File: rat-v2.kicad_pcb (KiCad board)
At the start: 2 copper layers, 56 x 60 mm, 57 parts, among them P1 9V, P2 LED-, P3 GND, P4 IN, P5 GND, P6 OUT, P7 GND, P8 GND, Q1 2N5458, SW1 SW_DPDT_x2, SW2 SW_DPDT_x2, U2 LM301

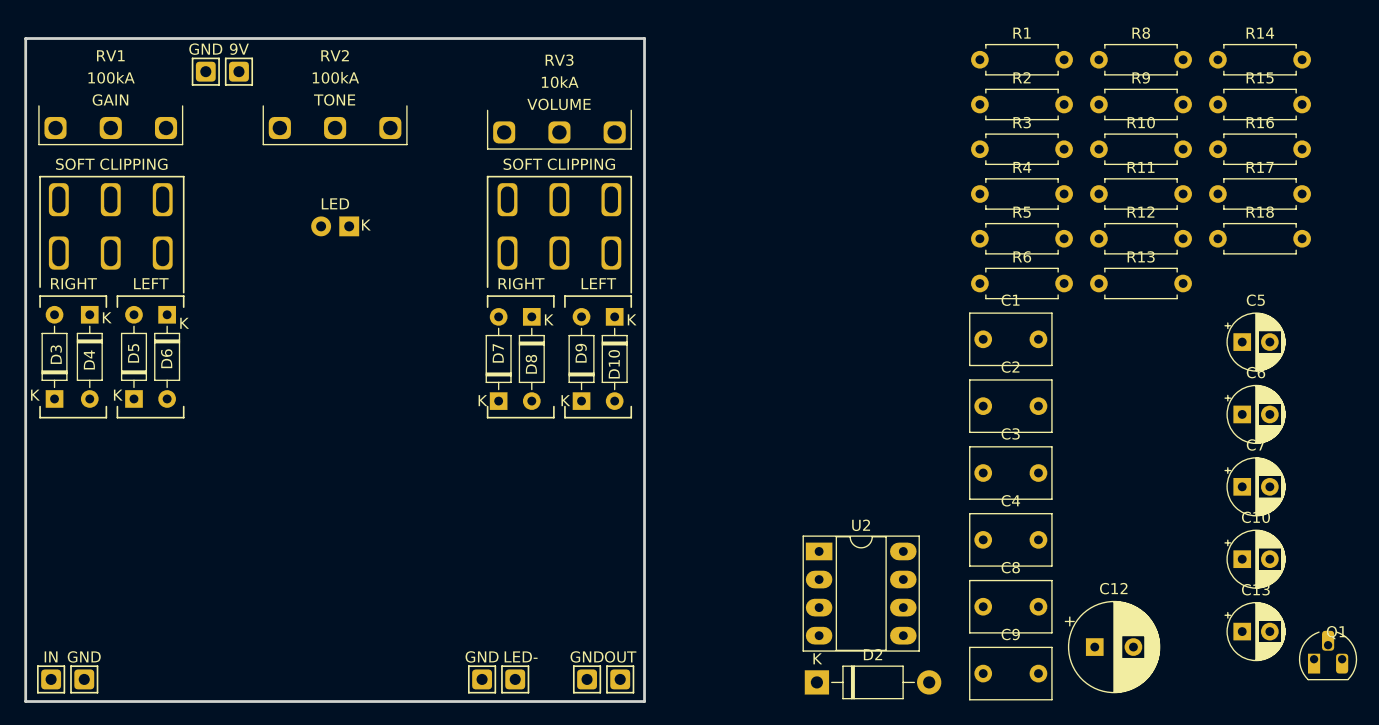
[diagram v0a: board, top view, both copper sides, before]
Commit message: Placement just about done
might need some minor tweaking
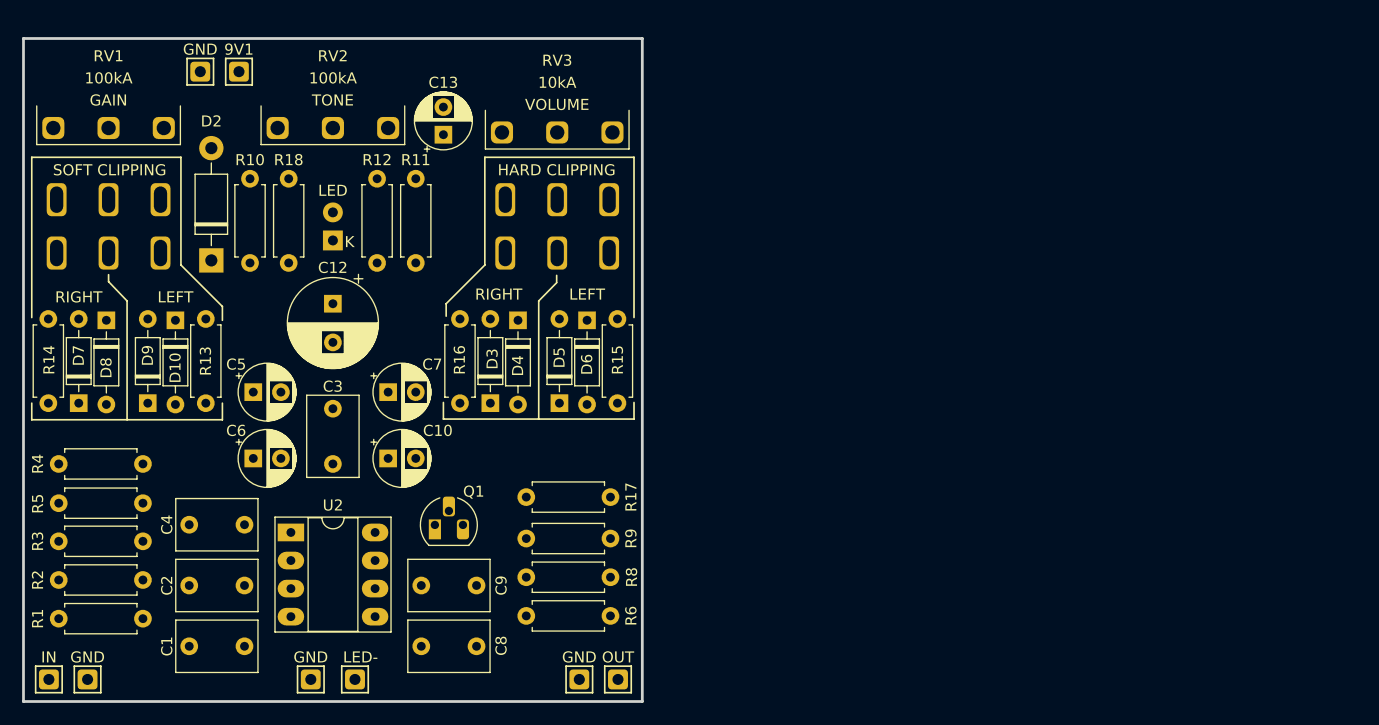
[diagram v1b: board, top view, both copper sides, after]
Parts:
- P1: value 9V -> 9V1
- moved R14 110.3 mm to (57.2, 114.0), turned to 90 degrees
- moved R1 97.5 mm to (58.2, 133.5)
- moved R3 90.6 mm to (58.2, 126.5)
- moved C5 89.6 mm to (75.8, 113.0)
- moved C6 89.6 mm to (75.8, 119.0)
- moved R2 87.1 mm to (65.8, 130.0), turned to 180 degrees
- moved C13 85.1 mm to (93.0, 89.7), turned to 90 degrees
- moved R18 84.3 mm to (79.0, 93.7), turned to -90 degrees
- moved R13 81.5 mm to (71.5, 114.0), turned to 90 degrees
- moved Q1 80.5 mm to (92.2, 125.0)
- moved R4 79.6 mm to (65.8, 119.5), turned to 180 degrees
- moved R5 79.4 mm to (65.8, 123.0), turned to 180 degrees
- moved C10 77.8 mm to (88.0, 119.0)
- moved C7 77.8 mm to (88.0, 113.0)
- moved R10 76.9 mm to (75.5, 93.7), turned to -90 degrees
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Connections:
- net Net-(C1-Pad1) renamed /IN
- net Net-(C1-Pad2) renamed /IN_AC
- net Net-(C10-Pad2) renamed /SRC_AC
- net Net-(C8-Pad2) renamed /TONE_F
- net Net-(D10-A) renamed /OP_OUT
- net Net-(P1-Pad1) renamed +9VIN
- net Net-(P6-Pad1) renamed /OUT
- net Net-(Q1-G) renamed /GATE
- net Net-(Q1-S) renamed /SRC
- net Net-(R6-Pad2) renamed /TONE
- net Net-(SW1A-B) renamed /HRD_CLP
- net Net-(SW2A-B) renamed /FB
- net Net-(U2-+) renamed /IN_F
- net Net-(U2-BAL) renamed /COMP-
- net Net-(U2-C/B) renamed /COMP+
- P8 pad 1: (no net) -> GND
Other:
- board text added: "HARD CLIPPING"

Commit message: Ship It?
I think it is finished. Error free. Haven't generated BOM or files
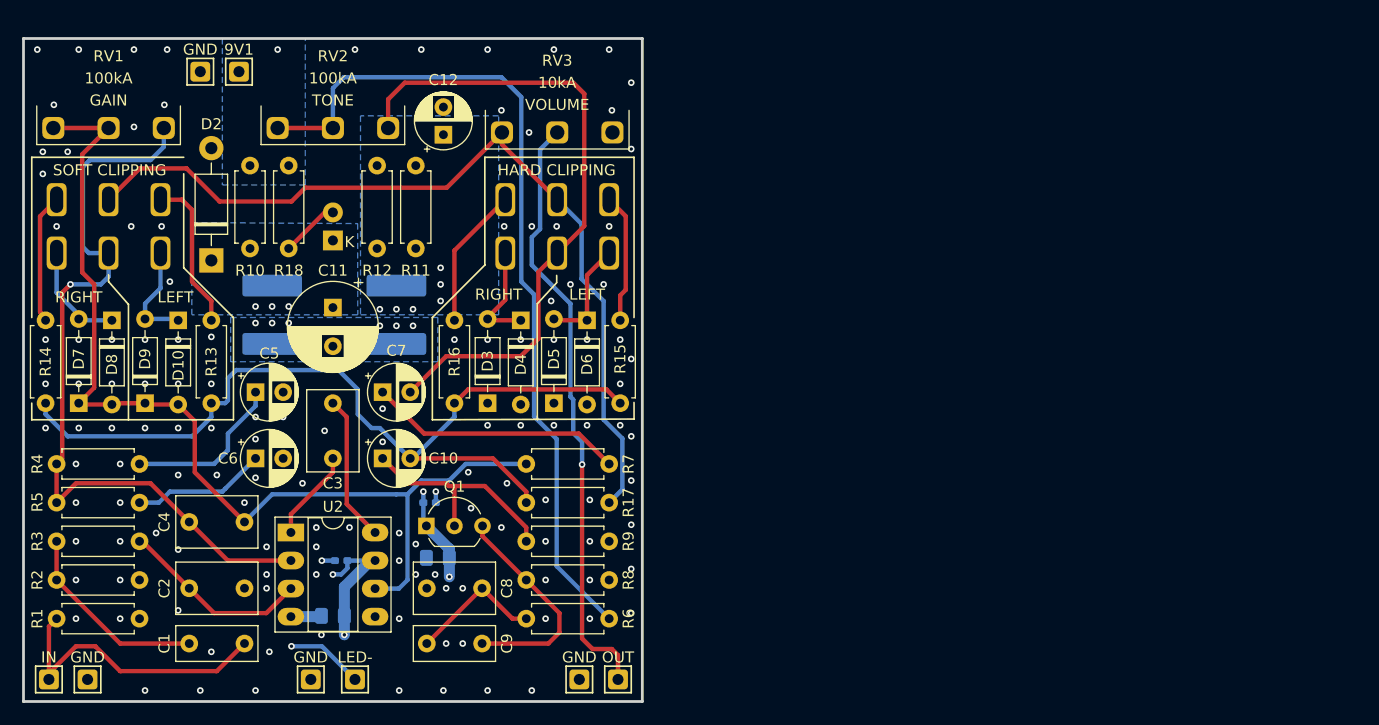
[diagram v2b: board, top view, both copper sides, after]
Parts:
- removed the REF** at (67.8, 52.0)
- removed the REF** at (98.2, 52.0)
- added C13: 1u, Capacitor_SMD:C_0805_2012Metric_Pad1.18x1.45mm_HandSolder, B.Cu at (83.0, 133.2)
- added C14: 1u, Capacitor_SMD:C_0805_2012Metric_Pad1.18x1.45mm_HandSolder, B.Cu at (92.5, 128.0)
- added C15: 100n, Capacitor_SMD:C_0402_1005Metric_Pad0.74x0.62mm_HandSolder, B.Cu at (83.8, 128.2)
- added C16: 100n, Capacitor_SMD:C_0402_1005Metric_Pad0.74x0.62mm_HandSolder, B.Cu at (91.8, 123.0)
- added C17: 10u, Capacitor_SMD:C_2220_5750Metric_Pad1.97x5.40mm_HandSolder, B.Cu at (77.5, 106.0)
- added C18: 10u, Capacitor_SMD:C_2220_5750Metric_Pad1.97x5.40mm_HandSolder, B.Cu at (88.8, 106.0)
- added R7: 1.5k, BB_Resistors:R_Axial_DIN0207_L6.3mm_D2.5mm_P7.5mm_Horizontal, F.Cu at (108.0, 119.5)
- added REF**: Jack_0.25in_Solder_MechOnly, BB_Jacks:Jack_0.25in_Solder_MechOnly, F.Cu at (98.4, 52.8)
- added REF**: Jack_0.25in_Solder_MechOnly, BB_Jacks:Jack_0.25in_Solder_MechOnly, F.Cu at (68.0, 52.8)
- C1, C9: footprint Capacitor_THT:C_Rect_L7.2mm_W4.5mm_P5.00mm_FKS2_FKP2_MKS2_MKP2 -> Capacitor_THT:C_Rect_L7.2mm_W3.0mm_P5.00mm_FKS2_FKP2_MKS2_MKP2
- C3: value 30p -> 47p
- Q1: footprint Package_TO_SOT_THT:TO-92_HandSolder -> Package_TO_SOT_THT:TO-92_Inline_Wide
- R1, R2: value 1M -> 2.2M; footprint Resistor_THT:R_Axial_DIN0207_L6.3mm_D2.5mm_P7.62mm_Horizontal -> BB_Resistors:R_Axial_DIN0207_L6.3mm_D2.5mm_P7.5mm_Horizontal
- R10, R11, R12, R13, R14, R15, R16, R17, R18, R3, R4, R5, R6, R8, R9: footprint Resistor_THT:R_Axial_DIN0207_L6.3mm_D2.5mm_P7.62mm_Horizontal -> BB_Resistors:R_Axial_DIN0207_L6.3mm_D2.5mm_P7.5mm_Horizontal
- moved C8 6.91 mm to (91.5, 130.8), turned to 0 degrees
- moved C9 5.27 mm to (91.5, 135.8)
- moved R12 1.31 mm to (87.0, 100.0)
- moved R10 1.19 mm to (75.5, 92.5)
- moved R11 1.19 mm to (90.5, 92.5)
- moved R18 1.19 mm to (79.0, 92.5)
- moved REF** 1.02 mm to (83.0, 51.0)
- moved Q1 0.78 mm to (91.5, 125.1)
- moved C10 0.50 mm to (87.5, 119.0)
- moved C3 0.50 mm to (83.0, 114.0)
- moved C7 0.50 mm to (87.5, 113.0)
- moved D5 0.50 mm to (103.0, 114.0)
- moved D8 0.50 mm to (63.0, 106.5)
- moved R13 0.50 mm to (72.0, 114.0)
- moved R16 0.50 mm to (94.0, 114.0)
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- renumbered C12 to C11, C13 to C12
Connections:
- C7 pad 1: /OP_OUT -> /OP_OUT_R
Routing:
- net /OP_OUT: track 0.00 -> 92.9 mm
- net /SRC_AC: track 0.00 -> 79.4 mm
- net Net-(SW1B-B): track 0.00 -> 79.1 mm
- net /TONE: track 0.00 -> 77.3 mm
- net Net-(D1-K): track 0.00 -> 72.2 mm, vias 0 -> 1
- net /FB: track 0.00 -> 71.2 mm, vias 0 -> 1
- net /HRD_CLP: track 0.00 -> 58.9 mm
- net /OUT: track 0.00 -> 54.7 mm, vias 0 -> 1
- net +9V: track 0.00 -> 31.1 mm, vias 0 -> 7
- net /IN: track 0.00 -> 27.0 mm
- net /OP_OUT_R: track 0.00 -> 23.8 mm
- net /SRC: track 0.00 -> 20.4 mm
- net /GATE: track 0.00 -> 19.9 mm
- net /IN_AC: track 0.00 -> 17.9 mm
- net /IN_F: track 0.00 -> 17.3 mm
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- added copper zone on B.Cu, net +4.5V
- added copper zone on In2.Cu, net +4.5V
- added copper zone on B.Cu, net +9V
- added copper zone on In2.Cu, net +9V
- added copper zone on B.Cu, net +9VIN
- added copper zone on B.Cu, net GND
- added copper zone on F.Cu, net GND
- added copper zone on In1.Cu, net GND
- added copper zone on In2.Cu, net GND
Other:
- copper layers 2 -> 4

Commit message: Few small edits, generated gerbers. Waiting for henry to order
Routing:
- net /FB: track 71.2 -> 74.6 mm
- net Net-(D1-A): track 5.35 -> 6.52 mm
- net GND: vias 142 -> 143
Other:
- board text added: "BLACK"
- board text added: "BOX"
- board text added: "EFFECTS"
- board text added: "RAT"
- board text added: "V2"
